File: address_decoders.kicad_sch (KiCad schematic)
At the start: 15 parts, among them U10 74LS74, U13 74LS32, U15 25LS2538PC, U19 74LS174, U3 74F04, U30 74LS157, U5 74LS08, U6 74LS32, U8 74LS373

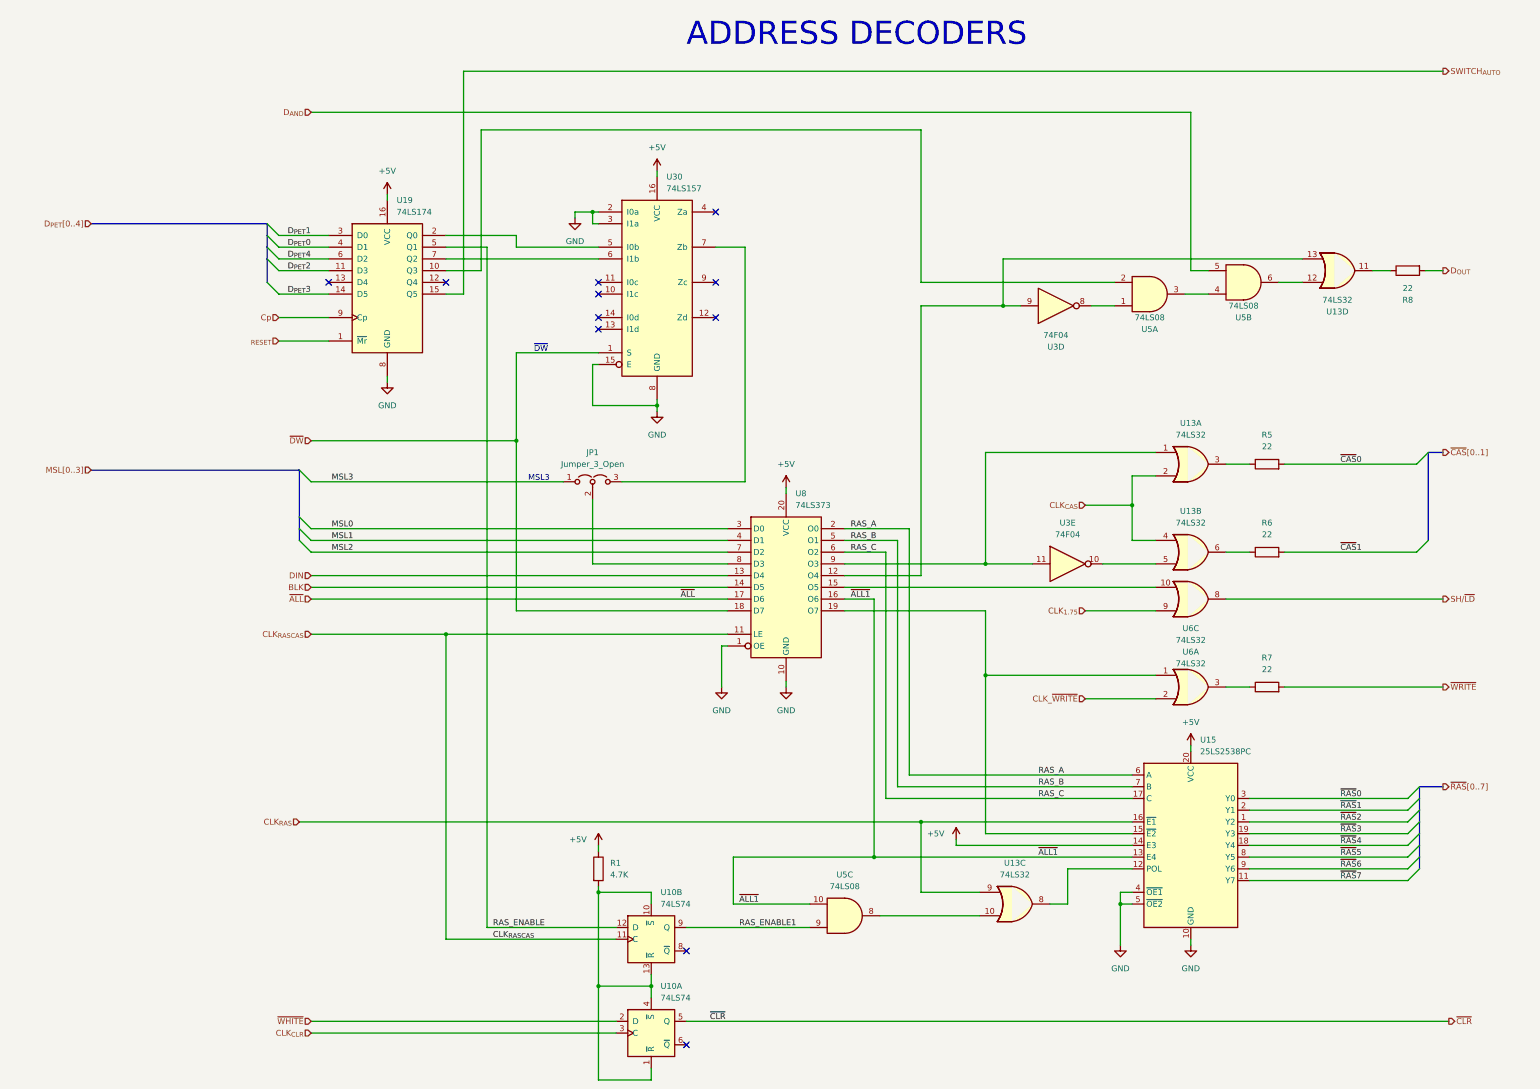
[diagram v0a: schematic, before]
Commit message: Improved signal naming
clearer naming of some signals for better readability
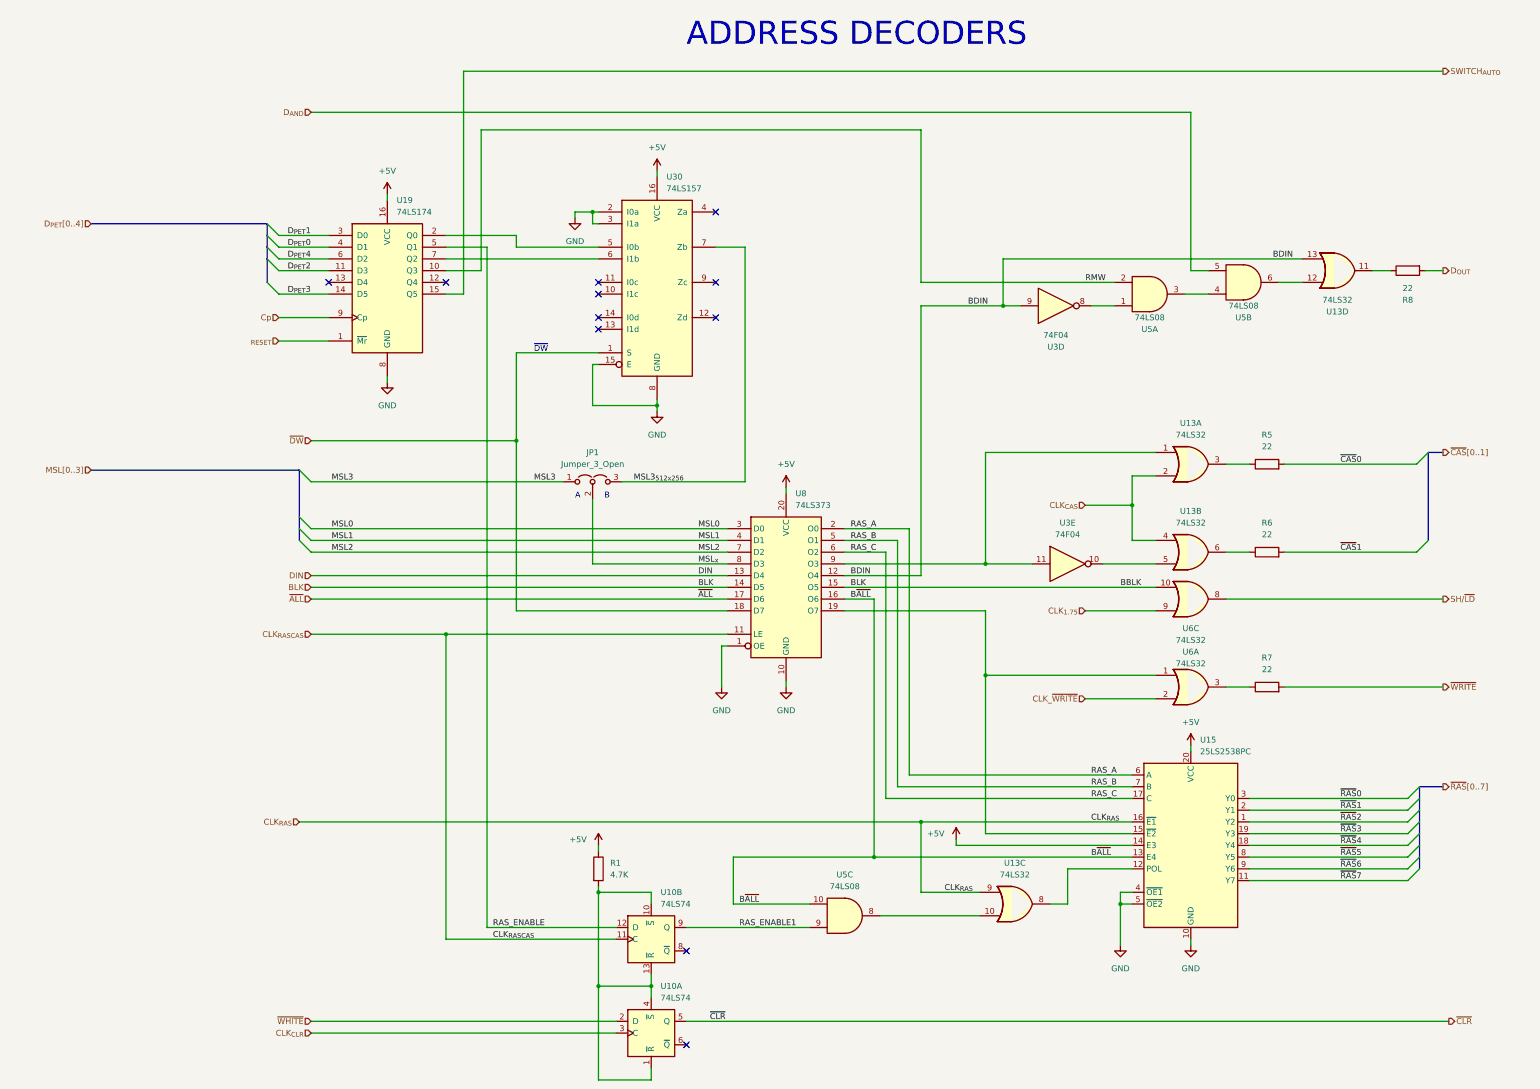
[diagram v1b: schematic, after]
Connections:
- net BLK: now also U6.10, U8.15 (O5)
- net BDIN: now reaches U13.13, U3.9, U8.12 (O4)
- net RMW: now reaches U19.10 (Q3), U5.2
- net MSL_{x}: now reaches JP1.2 (C), U8.8 (D3)
- net MSL3_{512x256}: now reaches JP1.3 (B), U30.7 (Zb)
- net ~{ALL1} renamed B~{ALL}
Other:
- note added: "A"
- note added: "B"
- note removed: "MSL3"
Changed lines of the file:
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@@
+    (stroke (width 0) (type default))
+  )
+  (wire (pts (xy 219.71 189.23) (xy 273.05 189.23))
     (stroke (width 0) (type default))
   )
@@
     (stroke (width 0) (type default))
   )
-  (wire (pts (xy 273.05 186.69) (xy 222.25 186.69))
-    (stroke (width 0) (type default))
-  )
   (wire (pts (xy 157.48 209.55) (xy 157.48 229.87))
     (stroke (width 0) (type default))
@@
     (stroke (width 0) (type default))
   )
-  (wire (pts (xy 273.05 189.23) (xy 219.71 189.23))
-    (stroke (width 0) (type default))
-  )
   (bus (pts (xy 85.725 77.47) (xy 85.725 72.39))
     (stroke (width 0) (type default))
@@
     (stroke (width 0) (type default))
   )
+  (wire (pts (xy 224.79 184.15) (xy 273.05 184.15))
+    (stroke (width 0) (type default))
+  )
   (wire (pts (xy 273.05 196.85) (xy 241.3 196.85))
     (stroke (width 0) (type default))
@@
     (stroke (width 0) (type default))
   )
-  (wire (pts (xy 224.79 184.15) (xy 273.05 184.15))
-    (stroke (width 0) (type default))
-  )
   (wire (pts (xy 95.25 111.76) (xy 139.7 111.76))
     (stroke (width 0) (type default))
@@
     (stroke (width 0) (type default))
   )
+  (wire (pts (xy 222.25 186.69) (xy 273.05 186.69))
+    (stroke (width 0) (type default))
+  )
   (wire (pts (xy 278.13 138.43) (xy 266.7 138.43))
     (stroke (width 0) (type default))
@@
   (wire (pts (xy 273.05 125.73) (xy 273.05 133.35))
     (stroke (width 0) (type default))
+  )
+  (text "A" (at 152.4 124.46 0)
+    (effects (font (size 1.27 1.27)) (justify left bottom))
   )
   (text "ADDRESS DECODERS" (at 176.53 26.67 0)
@@
     (effects (font (size 1.27 1.27)) (justify left bottom))
   )
-  (text "MSL3" (at 142.24 120.65 0)
+  (text "B" (at 158.75 124.46 0)
     (effects (font (size 1.27 1.27)) (justify left bottom))
   )
@@
     (effects (font (size 1.27 1.27)) (justify left bottom))
   )
+  (label "MSL2" (at 179.07 135.89 0) (fields_autoplaced)
+    (effects (font (size 1.27 1.27)) (justify left bottom))
+  )
+  (label "MSL1" (at 179.07 133.35 0) (fields_autoplaced)
+    (effects (font (size 1.27 1.27)) (justify left bottom))
+  )
   (label "RAS_ENABLE" (at 134.62 217.17 0) (fields_autoplaced)
     (effects (font (size 1.27 1.27)) (justify left bottom))
@@
     (effects (font (size 1.27 1.27)) (justify left bottom))
   )
+  (label "MSL3" (at 143.51 120.65 0) (fields_autoplaced)
+    (effects (font (size 1.27 1.27)) (justify left bottom))
+  )
   (label "D_{PET}0" (at 90.17 69.85 0) (fields_autoplaced)
     (effects (font (size 1.27 1.27)) (justify left bottom))
@@
     (effects (font (size 1.27 1.27)) (justify left bottom))
   )
-  (label "~{ALL}" (at 175.26 146.05 0) (fields_autoplaced)
+  (label "~{ALL}" (at 179.07 146.05 0) (fields_autoplaced)
     (effects (font (size 1.27 1.27)) (justify left bottom))
   )
@@
     (effects (font (size 1.27 1.27)) (justify left bottom))
   )
-  (label "RAS_C" (at 252.73 189.23 0) (fields_autoplaced)
+  (label "RAS_C" (at 264.16 189.23 0) (fields_autoplaced)
     (effects (font (size 1.27 1.27)) (justify left bottom))
   )
@@
     (effects (font (size 1.27 1.27)) (justify left bottom))
   )
-  (label "~{ALL1}" (at 187.96 212.09 0) (fields_autoplaced)
+  (label "B~{ALL}" (at 187.96 212.09 0) (fields_autoplaced)
     (effects (font (size 1.27 1.27)) (justify left bottom))
   )
@@
     (effects (font (size 1.27 1.27)) (justify left bottom))
   )
+  (label "BDIN" (at 237.49 82.55 0) (fields_autoplaced)
+    (effects (font (size 1.27 1.27)) (justify left bottom))
+  )
+  (label "DIN" (at 179.07 140.97 0) (fields_autoplaced)
+    (effects (font (size 1.27 1.27)) (justify left bottom))
+  )
   (label "~{RAS}5" (at 318.135 201.93 0) (fields_autoplaced)
     (effects (font (size 1.27 1.27)) (justify left bottom))
@@
     (effects (font (size 1.27 1.27)) (justify left bottom))
   )
-  (label "~{ALL1}" (at 212.09 146.05 0) (fields_autoplaced)
+  (label "BDIN" (at 212.09 140.97 0) (fields_autoplaced)
+    (effects (font (size 1.27 1.27)) (justify left bottom))
+  )
+  (label "B~{ALL}" (at 212.09 146.05 0) (fields_autoplaced)
     (effects (font (size 1.27 1.27)) (justify left bottom))
   )
@@
     (effects (font (size 1.27 1.27)) (justify left bottom))
   )
+  (label "MSL0" (at 179.07 130.81 0) (fields_autoplaced)
+    (effects (font (size 1.27 1.27)) (justify left bottom))
+  )
   (label "~{RAS}0" (at 318.135 189.23 0) (fields_autoplaced)
     (effects (font (size 1.27 1.27)) (justify left bottom))
   )
+  (label "BLK" (at 212.09 143.51 0) (fields_autoplaced)
+    (effects (font (size 1.27 1.27)) (justify left bottom))
+  )
   (label "~{RAS}3" (at 318.135 196.85 0) (fields_autoplaced)
     (effects (font (size 1.27 1.27)) (justify left bottom))
@@
     (effects (font (size 1.27 1.27)) (justify left bottom))
   )
-  (label "RAS_A" (at 252.73 184.15 0) (fields_autoplaced)
+  (label "RAS_A" (at 264.16 184.15 0) (fields_autoplaced)
     (effects (font (size 1.27 1.27)) (justify left bottom))
   )
@@
     (effects (font (size 1.27 1.27)) (justify left bottom))
   )
+  (label "MSL_{x}" (at 179.07 138.43 0) (fields_autoplaced)
+    (effects (font (size 1.27 1.27)) (justify left bottom))
+  )
   (label "RAS_B" (at 212.09 133.35 0) (fields_autoplaced)
     (effects (font (size 1.27 1.27)) (justify left bottom))
   )
+  (label "BLK" (at 179.07 143.51 0) (fields_autoplaced)
+    (effects (font (size 1.27 1.27)) (justify left bottom))
+  )
   (label "D_{PET}3" (at 90.17 80.01 0) (fields_autoplaced)
     (effects (font (size 1.27 1.27)) (justify left bottom))
   )
-  (label "RAS_B" (at 252.73 186.69 0) (fields_autoplaced)
-    (effects (font (size 1.27 1.27)) (justify left bottom))
-  )
-  (label "~{ALL1}" (at 252.73 201.93 0) (fields_autoplaced)
+  (label "RAS_B" (at 264.16 186.69 0) (fields_autoplaced)
+    (effects (font (size 1.27 1.27)) (justify left bottom))
+  )
+  (label "BDIN" (at 303.53 72.39 0) (fields_autoplaced)
+    (effects (font (size 1.27 1.27)) (justify left bottom))
+  )
+  (label "B~{ALL}" (at 264.16 201.93 0) (fields_autoplaced)
+    (effects (font (size 1.27 1.27)) (justify left bottom))
+  )
+  (label "RMW" (at 262.89 77.47 0) (fields_autoplaced)
+    (effects (font (size 1.27 1.27)) (justify left bottom))
+  )
+  (label "CLK_{RAS}" (at 232.41 209.55 0) (fields_autoplaced)
+    (effects (font (size 1.27 1.27)) (justify left bottom))
+  )
+  (label "MSL3_{512x256}" (at 165.1 120.65 0) (fields_autoplaced)
+    (effects (font (size 1.27 1.27)) (justify left bottom))
+  )
+  (label "CLK_{RAS}" (at 264.16 194.31 0) (fields_autoplaced)
     (effects (font (size 1.27 1.27)) (justify left bottom))
   )
@@
     (effects (font (size 1.27 1.27)) (justify left bottom))
   )
+  (label "BBLK" (at 270.51 143.51 0) (fields_autoplaced)
+    (effects (font (size 1.27 1.27)) (justify left bottom))
+  )
